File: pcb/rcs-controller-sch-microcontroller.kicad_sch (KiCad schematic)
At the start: 33 parts, among them J4 Screw_Terminal_4_P3.50mm, J5 USB_C_Receptacle_USB2.0_14P, J6 Conn_01x03, Q2 SI7465DP-T1-E3, Q3 SI7465DP-T1-E3, Q4 PMV45EN2, Q5 PMV45EN2, SW1 SW_Push, U1 LSM6DSOX, U4 ESP32-S3-WROOM-1

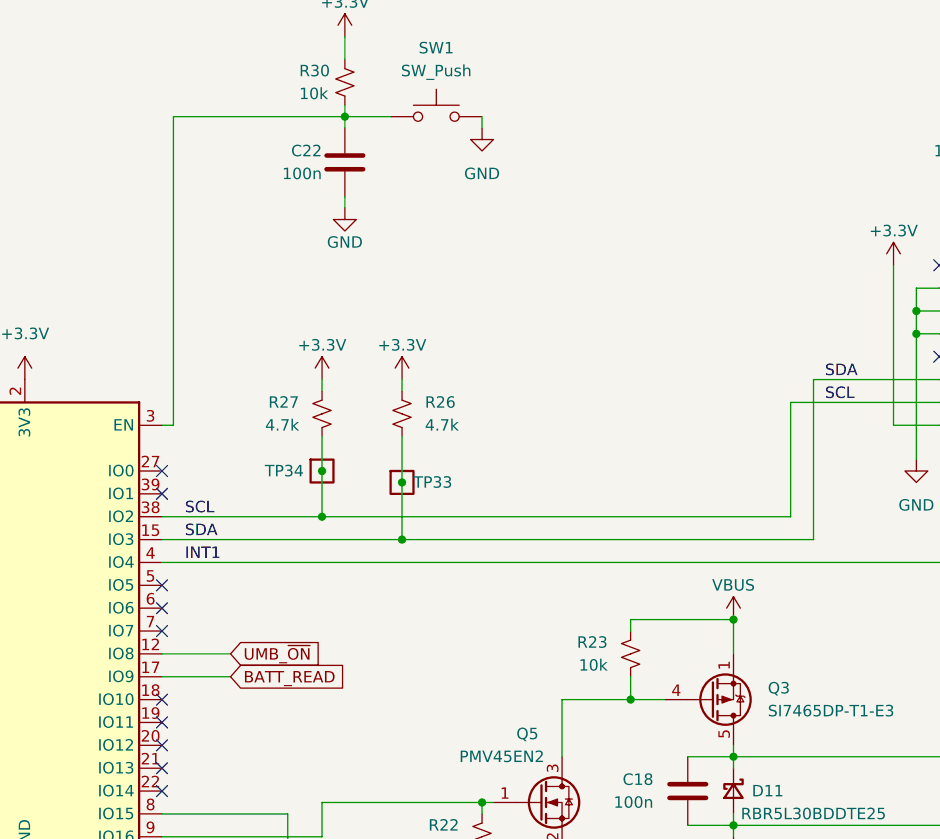
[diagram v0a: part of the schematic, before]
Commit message: added debug led and boot button
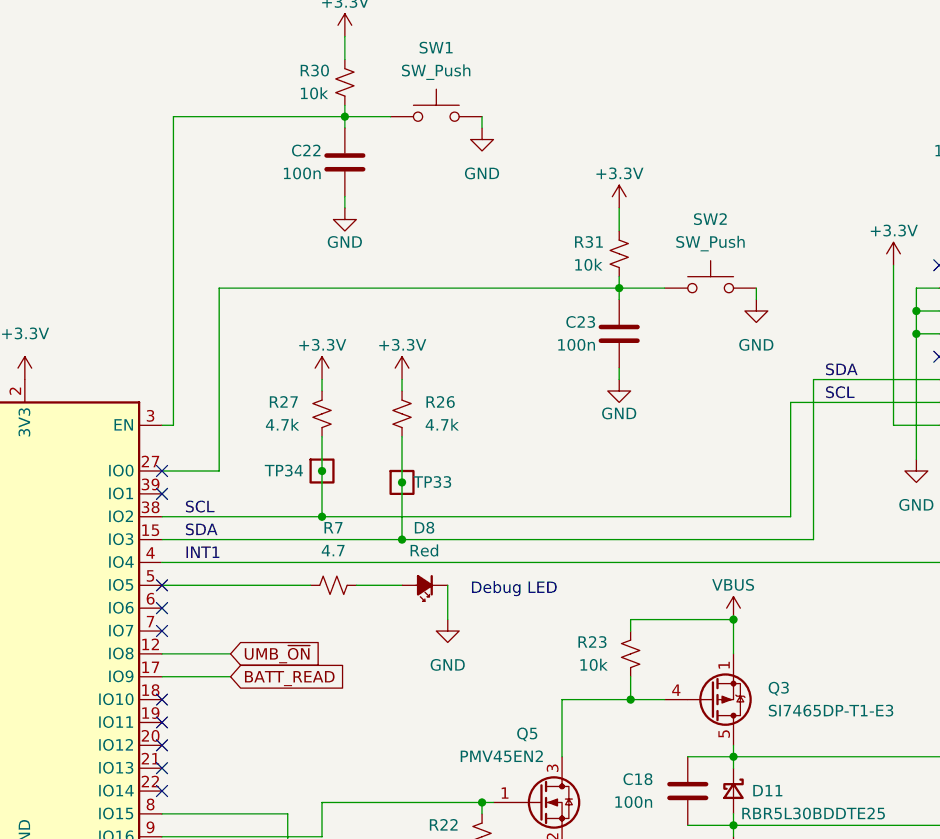
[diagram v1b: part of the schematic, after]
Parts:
- added C23: 100n, Capacitor_SMD:C_0603_1608Metric, symbol Device:C
- added D8: Red, LED_SMD:LED_0603_1608Metric, symbol Device:LED_Small_Filled
- added R31: 10k, Resistor_SMD:R_0603_1608Metric, symbol Device:R_Small_US
- added R7: 4.7, Resistor_SMD:R_0603_1608Metric, symbol Device:R_Small_US
- added SW2: SW_Push, Button_Switch_THT:SW_PUSH_6mm, symbol Switch:SW_Push
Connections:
- net +3.3V: now also R31.1
- net GND: now also C23.2, D8.1 (K), SW2.2
- net at U4.27 (IO0): now also C23.1, R31.2, SW2.1
- net at U4.5 (IO5): now also R7.1
- new net: D8.2 (A), R7.2
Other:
- note added: "Debug LED"

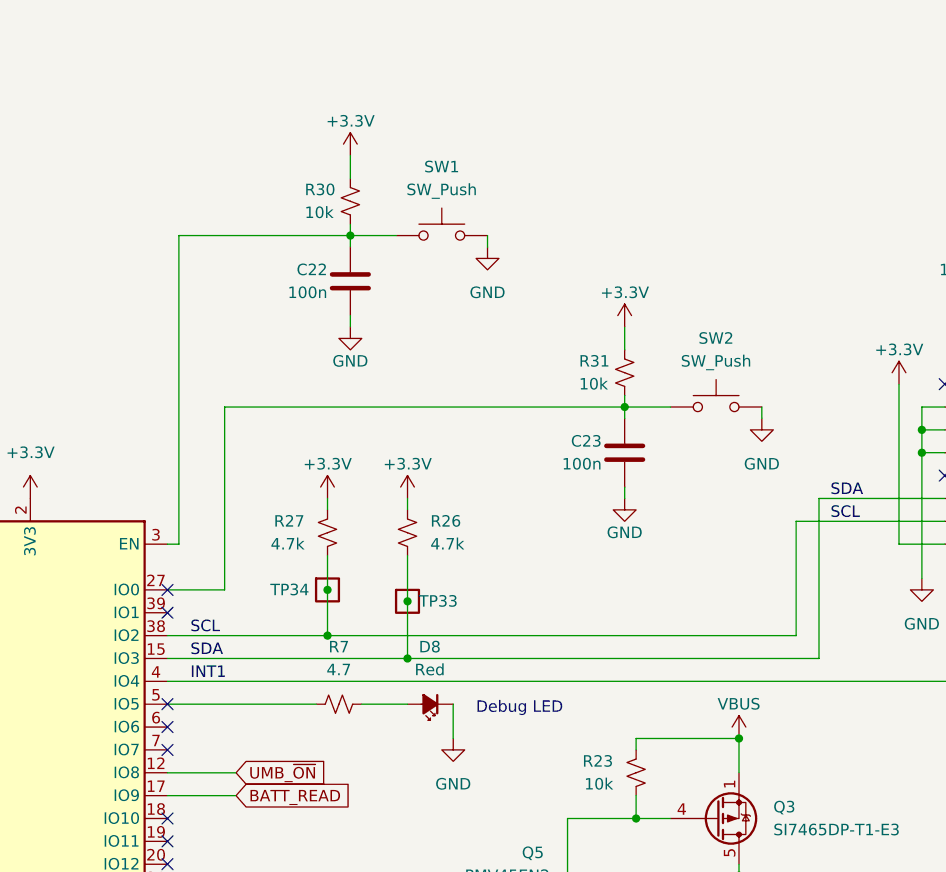
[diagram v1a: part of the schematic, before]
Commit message: Removed no connect flags to address warnings
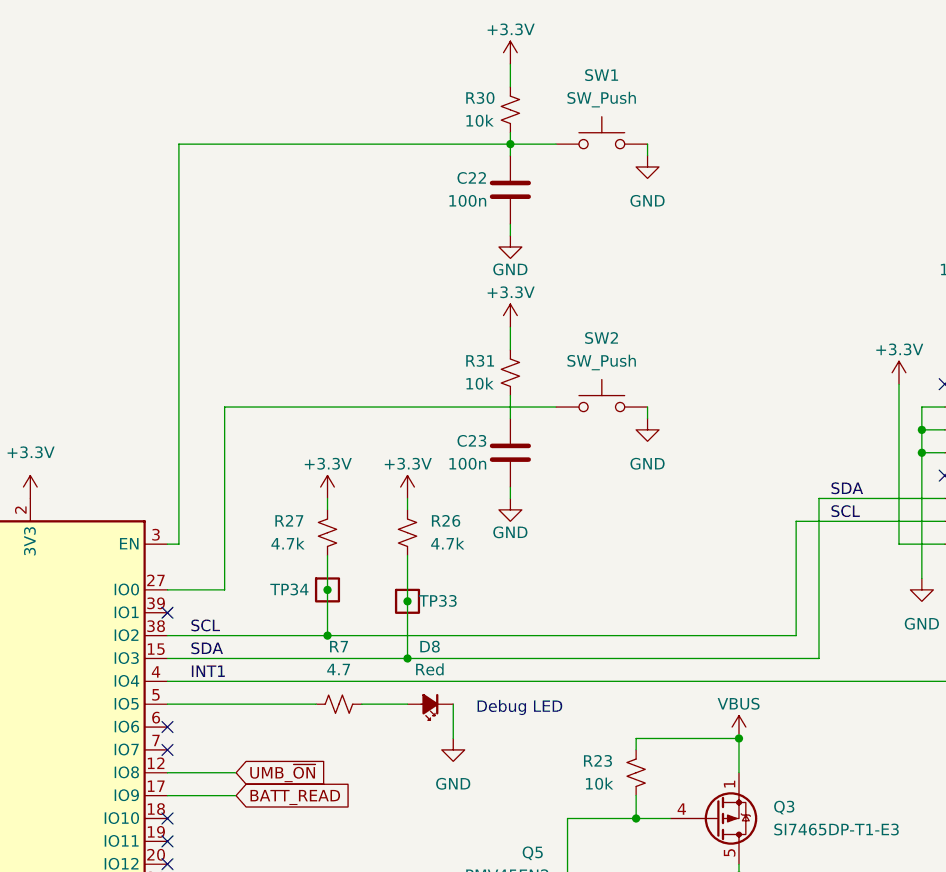
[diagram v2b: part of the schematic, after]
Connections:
- net at C23.1, R31.2: no longer SW2.1, U4.27 (IO0)
- new net: SW2.1, U4.27 (IO0)
- no-connect marks 29 -> 27
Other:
- moved on the sheet: C22, C23, R30, R31, SW1, SW2

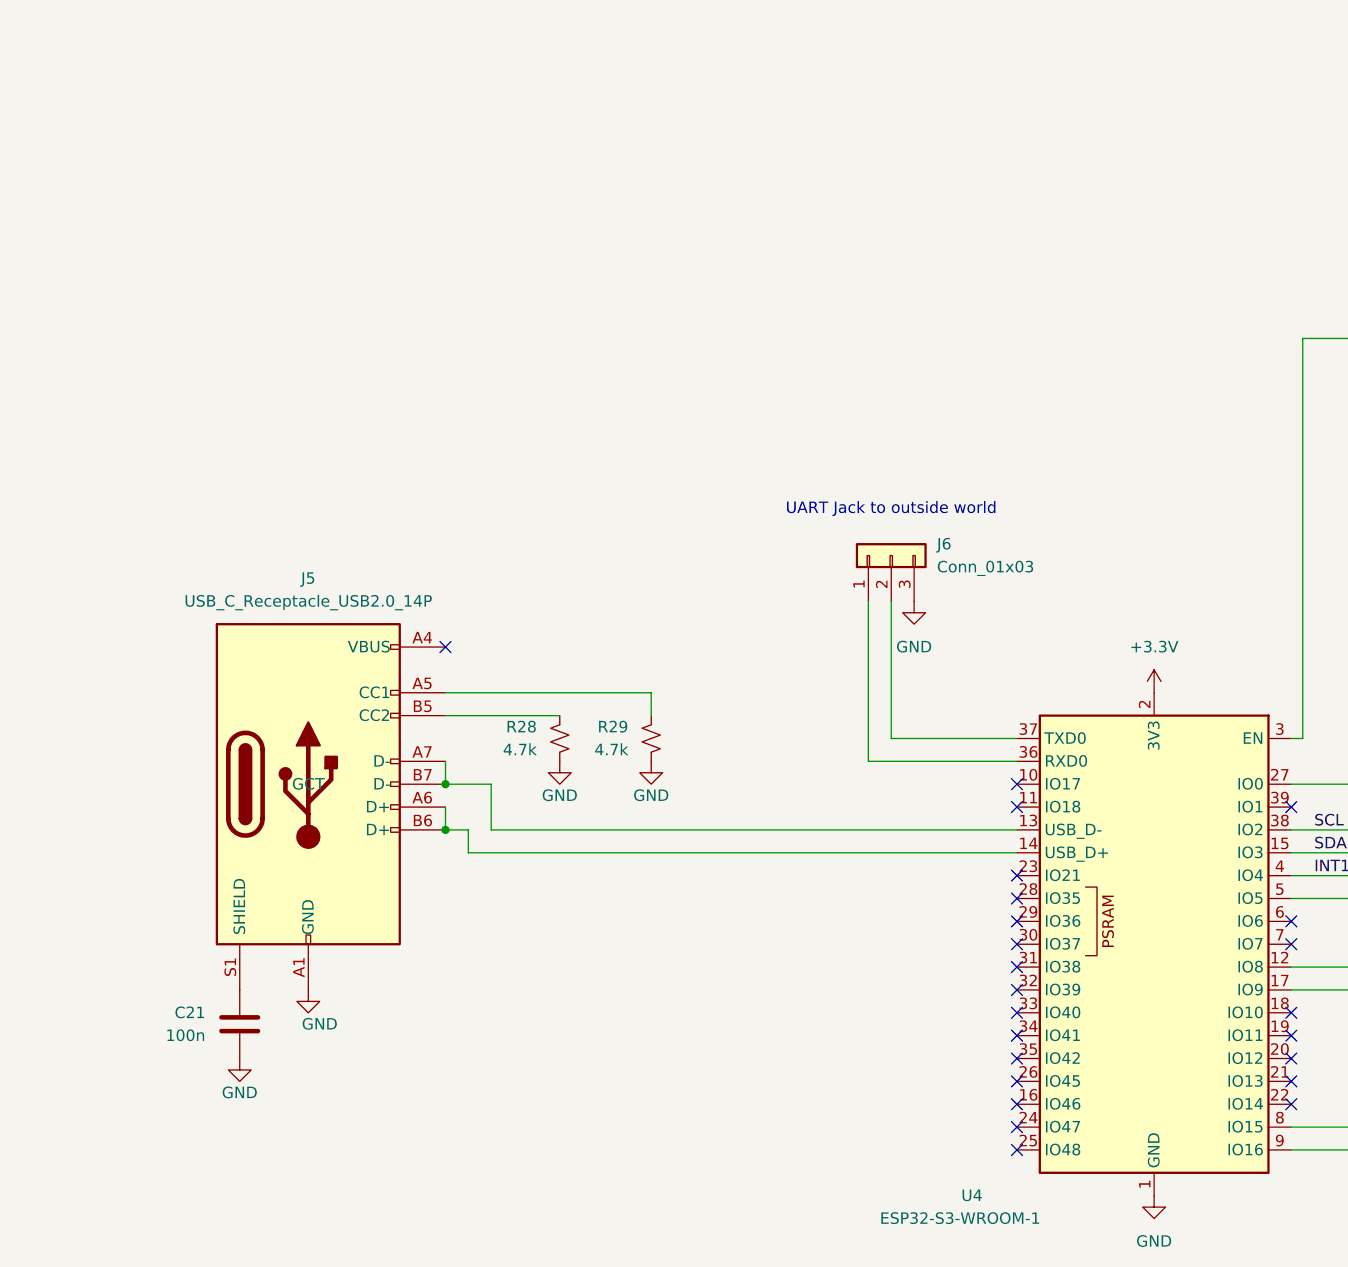
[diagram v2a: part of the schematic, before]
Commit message: Potential switching circuit between battery and USB
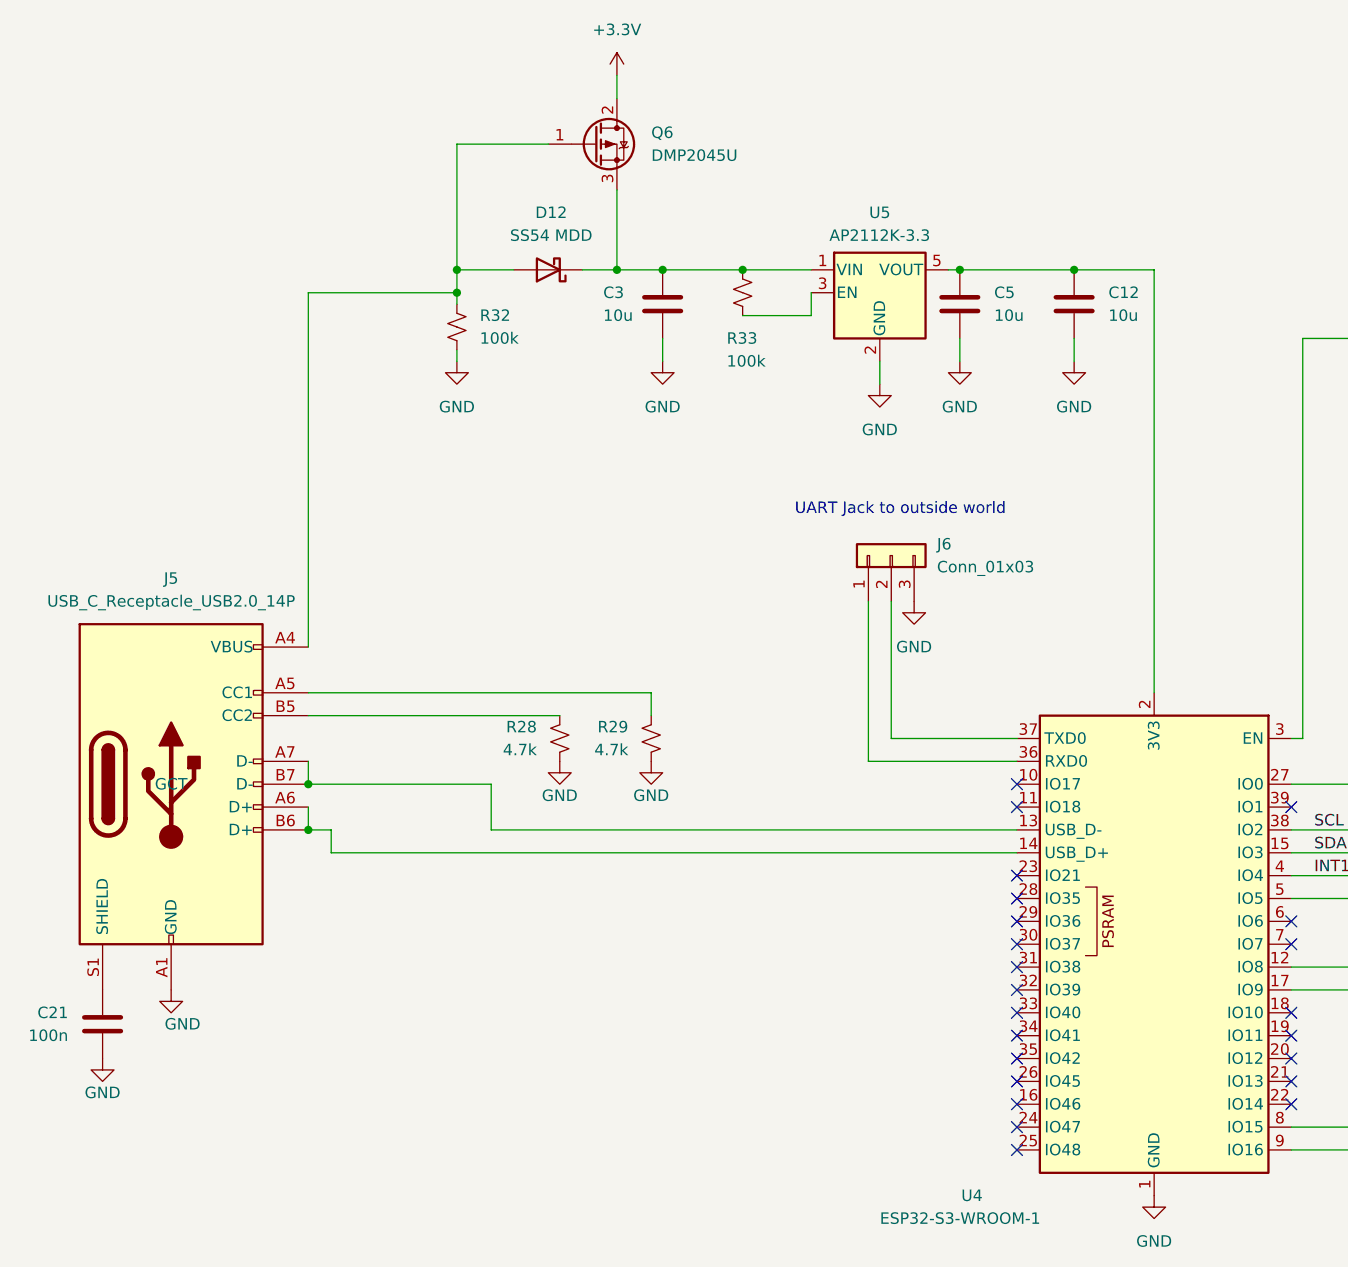
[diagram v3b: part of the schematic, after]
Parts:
- added C12, C3, C5: 10u, symbol Device:C
- added D12: SS54 MDD, symbol Device:D_Schottky
- added Q6: DMP2045U, Package_TO_SOT_SMD:TO-252-2, symbol Transistor_FET:SUD08P06-155L
- added R32, R33: 100k, symbol Device:R_Small_US
- added U5: AP2112K-3.3, Package_TO_SOT_SMD:SOT-23-5, symbol Regulator_Linear:AP2112K-3.3
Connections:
- net +3.3V: now also Q6.2 (D); no longer U4.2 (3V3)
- net GND: now also C12.2, C3.2, C5.2, R32.2, U5.2 (GND)
- net at J5.A4 (VBUS), J5.A9 (VBUS), J5.B4 (VBUS)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: now also D12.2 (A), Q6.1 (G), R32.1
- new net: C3.1, D12.1 (K), Q6.3 (S), R33.1, U5.1 (VIN)
- new net: R33.2, U5.3 (EN)
- new net: C12.1, C5.1, U4.2 (3V3), U5.5 (VOUT)
- no-connect marks 27 -> 26
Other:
- moved on the sheet: C21, J5
